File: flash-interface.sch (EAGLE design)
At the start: 2 parts, among them IC1 STM32L412K8U6, IC2 W25N01GVZEIG_TR

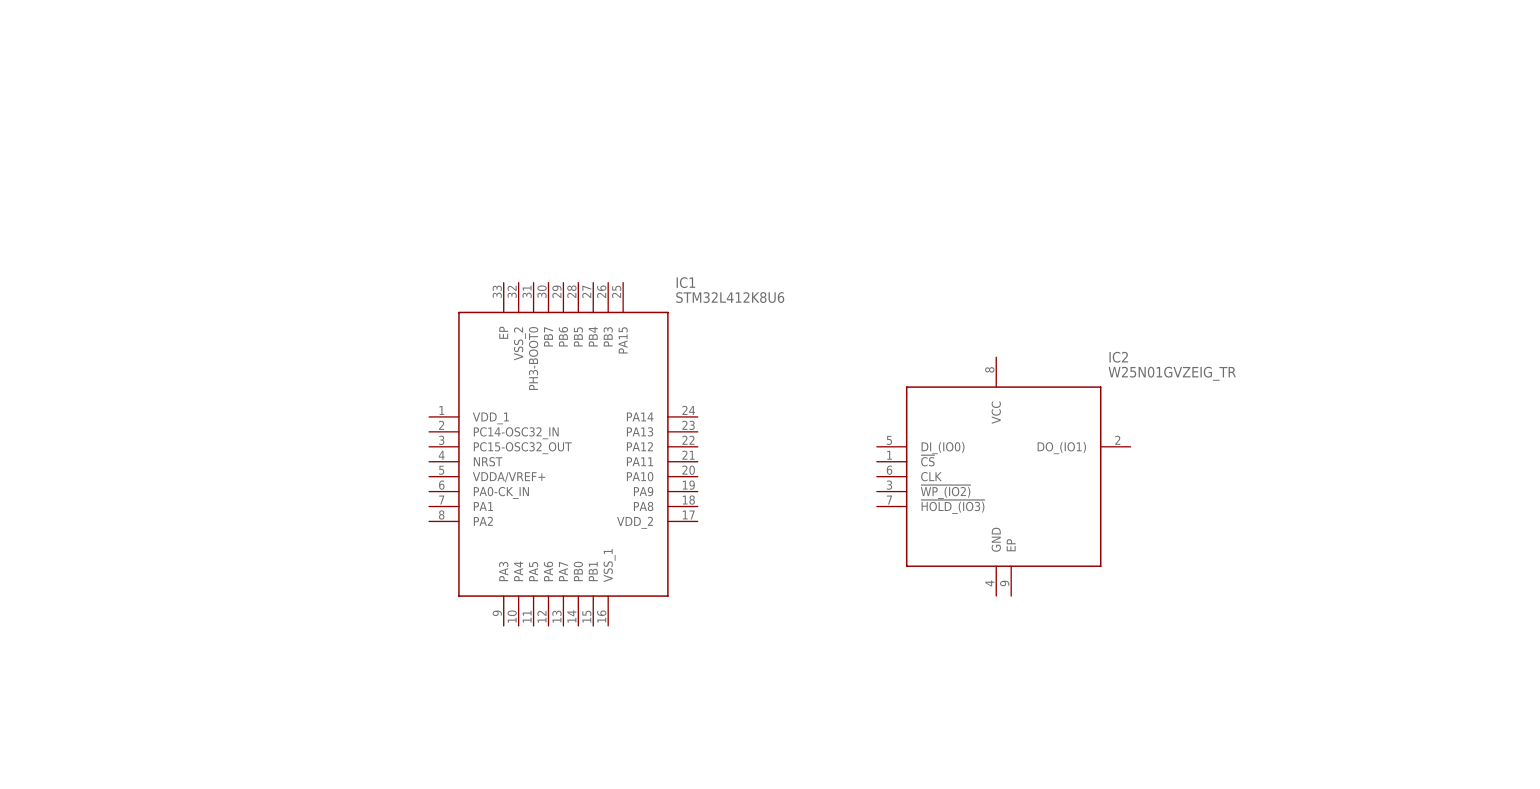
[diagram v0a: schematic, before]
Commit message: Added bare minimum components for both ICs
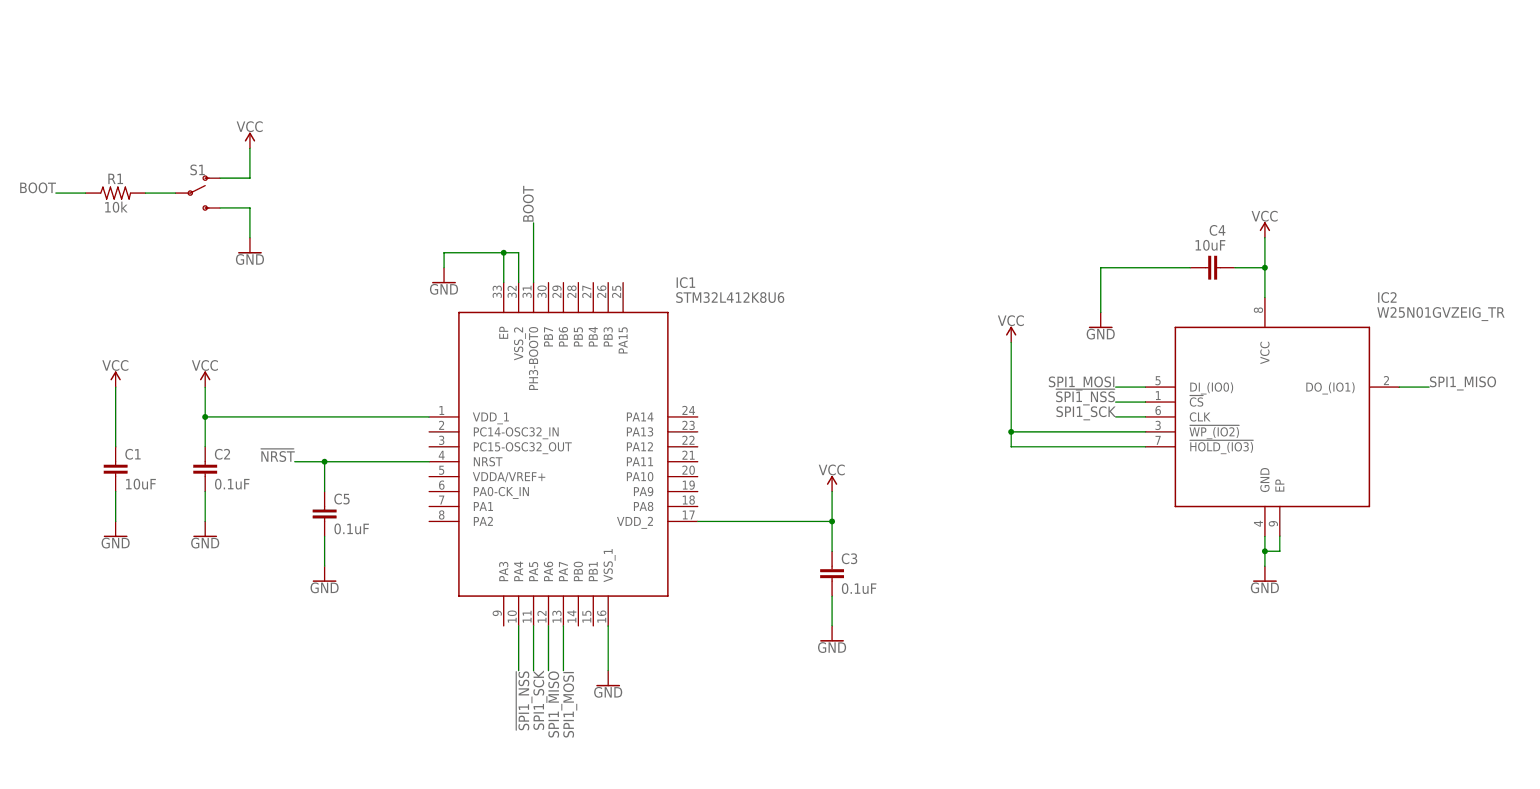
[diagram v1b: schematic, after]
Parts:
- added C1, C4: 10uF, SparkFun-Capacitors:10UF-0603-6.3V-20%
- added C2, C3, C5: 0.1uF, SparkFun-Capacitors:0.1UF-0603-25V-(+80/-20%)
- added R1: 10k, SparkFun-Resistors:10KOHM-0603-1/10W-1%
- added S1: (no value), SparkFun-Switches:SWITCH-SPDT-SMD-AYZ0202
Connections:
- new net !NRST: C5.1, IC1.NRST
- new net !SPI1_NSS: IC1.PA4, IC2.!CS
- new net BOOT: IC1.PH3-BOOT0, R1.1
- new net GND: C1.2, C2.2, C3.2, C4.2, C5.2, IC1.EP, IC1.VSS_1, IC1.VSS_2, IC2.EP, IC2.GND, S1.S
- new net N$1: R1.2, S1.P
- new net SPI1_MISO: IC1.PA6, IC2.DO_(IO1)
- new net SPI1_MOSI: IC1.PA7, IC2.DI_(IO0)
- new net SPI1_SCK: IC1.PA5, IC2.CLK
- new net VCC: C1.1, C2.1, C3.1, C4.1, IC1.VDD_1, IC1.VDD_2, IC2.!HOLD_(IO3), IC2.!WP_(IO2), IC2.VCC, S1.O
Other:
- moved on the sheet: IC2

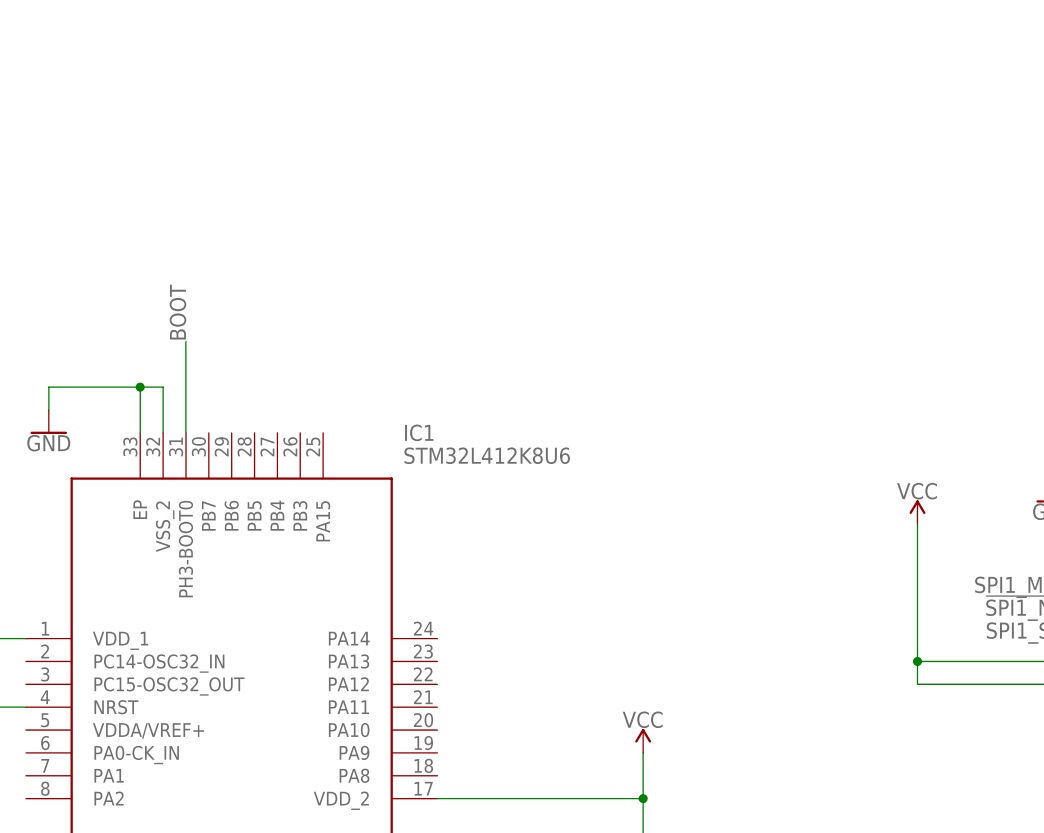
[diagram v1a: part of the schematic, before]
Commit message: Added SWD debug connector to STM32
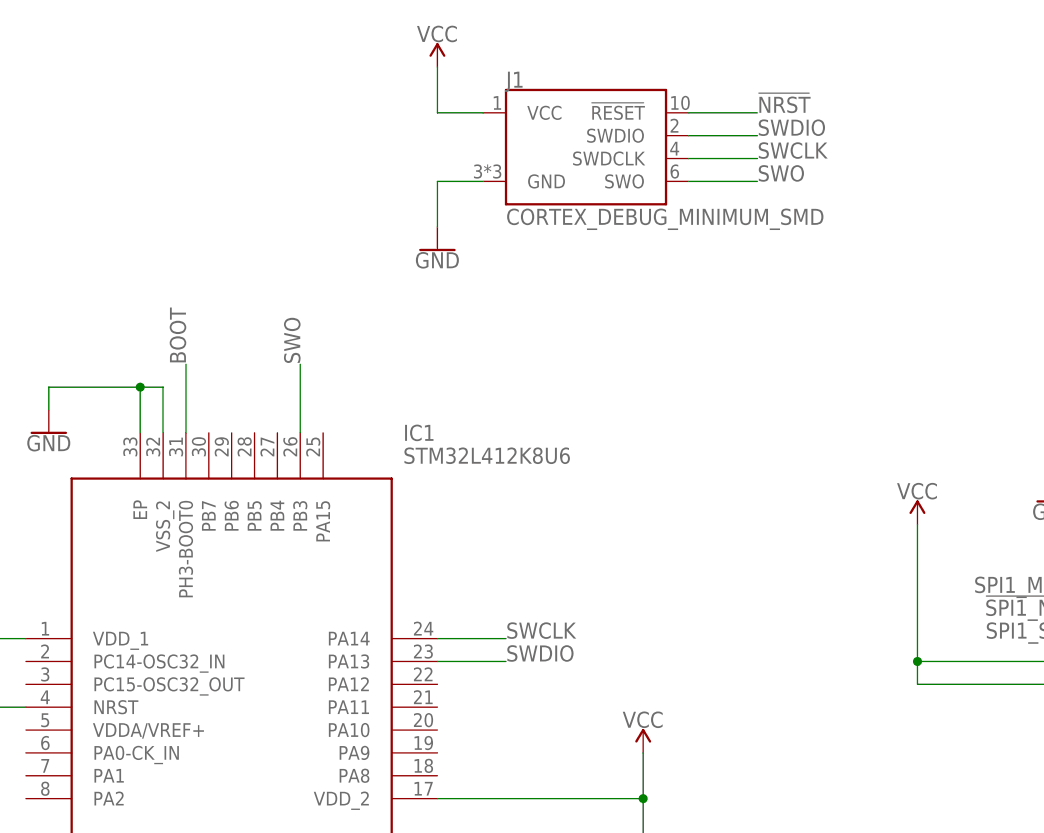
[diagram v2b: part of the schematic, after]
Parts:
- added J1: CORTEX_DEBUG_MINIMUM_SMD, SparkFun-Connectors:CORTEX_DEBUG_MINIMUM_SMD
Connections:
- new net SWCLK: IC1.PA14, J1.SWDCLK
- new net SWDIO: IC1.PA13, J1.SWDIO
- new net SWO: IC1.PB3, J1.SWO
- net !NRST: now also J1.!RESET
- net GND: now also J1.GND
- net VCC: now also J1.VCC
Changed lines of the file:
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@@
 <layer number="230" name="230bmp" color="7" fill="1" visible="yes" active="yes"/>
 <layer number="231" name="231bmp" color="7" fill="1" visible="yes" active="yes"/>
+<layer number="232" name="Eagle3D_PG2" color="7" fill="1" visible="no" active="no"/>
+<layer number="233" name="Eagle3D_PG3" color="7" fill="1" visible="no" active="no"/>
 <layer number="248" name="Housing" color="7" fill="1" visible="yes" active="yes"/>
 <layer number="249" name="Edge" color="7" fill="1" visible="yes" active="yes"/>
@@
 <part name="SUPPLY6" library="SparkFun-PowerSymbols" library_urn="urn:adsk.eagle:library:530" deviceset="VCC" device=""/>
 <part name="GND9" library="SparkFun-PowerSymbols" library_urn="urn:adsk.eagle:library:530" deviceset="GND" device=""/>
+<part name="J1" library="SparkFun-Connectors" deviceset="CORTEX_DEBUG_MINIMUM" device="_SMD"/>
+<part name="GND10" library="SparkFun-PowerSymbols" library_urn="urn:adsk.eagle:library:530" deviceset="GND" device=""/>
+<part name="SUPPLY7" library="SparkFun-PowerSymbols" library_urn="urn:adsk.eagle:library:530" deviceset="VCC" device=""/>
 </parts>
 <sheets>
@@
 <attribute name="VALUE" x="5.08" y="83.566" size="1.778" layer="96" align="top-center"/>
 </instance>
+<instance part="J1" gate="G$1" x="99.06" y="109.22" smashed="yes">
+<attribute name="NAME" x="88.9" y="117.094" size="1.778" layer="95" font="vector"/>
+<attribute name="VALUE" x="88.9" y="101.854" size="1.778" layer="96" font="vector"/>
+</instance>
+<instance part="GND10" gate="1" x="81.28" y="99.06" smashed="yes">
+<attribute name="VALUE" x="81.28" y="98.806" size="1.778" layer="96" align="top-center"/>
+</instance>
+<instance part="SUPPLY7" gate="G$1" x="81.28" y="119.38" smashed="yes">
+<attribute name="VALUE" x="81.28" y="122.174" size="1.778" layer="96" align="bottom-center"/>
+</instance>
 </instances>
 <busses>
@@
 <pinref part="GND9" gate="1" pin="GND"/>
 </segment>
+<segment>
+<pinref part="GND10" gate="1" pin="GND"/>
+<wire x1="81.28" y1="101.6" x2="81.28" y2="106.68" width="0.1524" layer="91"/>
+<pinref part="J1" gate="G$1" pin="GND"/>
+<wire x1="81.28" y1="106.68" x2="86.36" y2="106.68" width="0.1524" layer="91"/>
+</segment>
 </net>
 <net name="VCC" class="0">
@@
 <pinref part="SUPPLY6" gate="G$1" pin="VCC"/>
 </segment>
+<segment>
+<pinref part="SUPPLY7" gate="G$1" pin="VCC"/>
+<wire x1="81.28" y1="119.38" x2="81.28" y2="114.3" width="0.1524" layer="91"/>
+<pinref part="J1" gate="G$1" pin="VCC"/>
+<wire x1="81.28" y1="114.3" x2="86.36" y2="114.3" width="0.1524" layer="91"/>
+</segment>
 </net>
 <net name="!NRST" class="0">
@@
 <label x="12.7" y="48.26" size="1.778" layer="95" rot="MR0"/>
 </segment>
+<segment>
+<pinref part="J1" gate="G$1" pin="!RESET"/>
+<wire x1="109.22" y1="114.3" x2="116.84" y2="114.3" width="0.1524" layer="91"/>
+<label x="116.84" y="114.3" size="1.778" layer="95"/>
+</segment>
 </net>
 <net name="BOOT" class="0">
 <segment>
 <pinref part="IC1" gate="G$1" pin="PH3-BOOT0"/>
-<wire x1="53.34" y1="78.74" x2="53.34" y2="88.9" width="0.1524" layer="91"/>
-<label x="53.34" y="88.9" size="1.778" layer="95" rot="R90"/>
+<wire x1="53.34" y1="78.74" x2="53.34" y2="86.36" width="0.1524" layer="91"/>
+<label x="53.34" y="86.36" size="1.778" layer="95" rot="R90"/>
 </segment>
 <segment>
@@
 </segment>
 </net>
+<net name="SWDIO" class="0">
+<segment>
+<pinref part="IC1" gate="G$1" pin="PA13"/>
+<wire x1="81.28" y1="53.34" x2="88.9" y2="53.34" width="0.1524" layer="91"/>
+<label x="88.9" y="53.34" size="1.778" layer="95"/>
+</segment>
+<segment>
+<pinref part="J1" gate="G$1" pin="SWDIO"/>
+<wire x1="109.22" y1="111.76" x2="116.84" y2="111.76" width="0.1524" layer="91"/>
+<label x="116.84" y="111.76" size="1.778" layer="95"/>
+</segment>
+</net>
+<net name="SWCLK" class="0">
+<segment>
+<pinref part="IC1" gate="G$1" pin="PA14"/>
+<wire x1="81.28" y1="55.88" x2="88.9" y2="55.88" width="0.1524" layer="91"/>
+<label x="88.9" y="55.88" size="1.778" layer="95"/>
+</segment>
+<segment>
+<pinref part="J1" gate="G$1" pin="SWDCLK"/>
+<wire x1="109.22" y1="109.22" x2="116.84" y2="109.22" width="0.1524" layer="91"/>
+<label x="116.84" y="109.22" size="1.778" layer="95"/>
+</segment>
+</net>
+<net name="SWO" class="0">
+<segment>
+<pinref part="IC1" gate="G$1" pin="PB3"/>
+<wire x1="66.04" y1="78.74" x2="66.04" y2="86.36" width="0.1524" layer="91"/>
+<label x="66.04" y="86.36" size="1.778" layer="95" rot="R90"/>
+</segment>
+<segment>
+<pinref part="J1" gate="G$1" pin="SWO"/>
+<wire x1="109.22" y1="106.68" x2="116.84" y2="106.68" width="0.1524" layer="91"/>
+<label x="116.84" y="106.68" size="1.778" layer="95"/>
+</segment>
+</net>

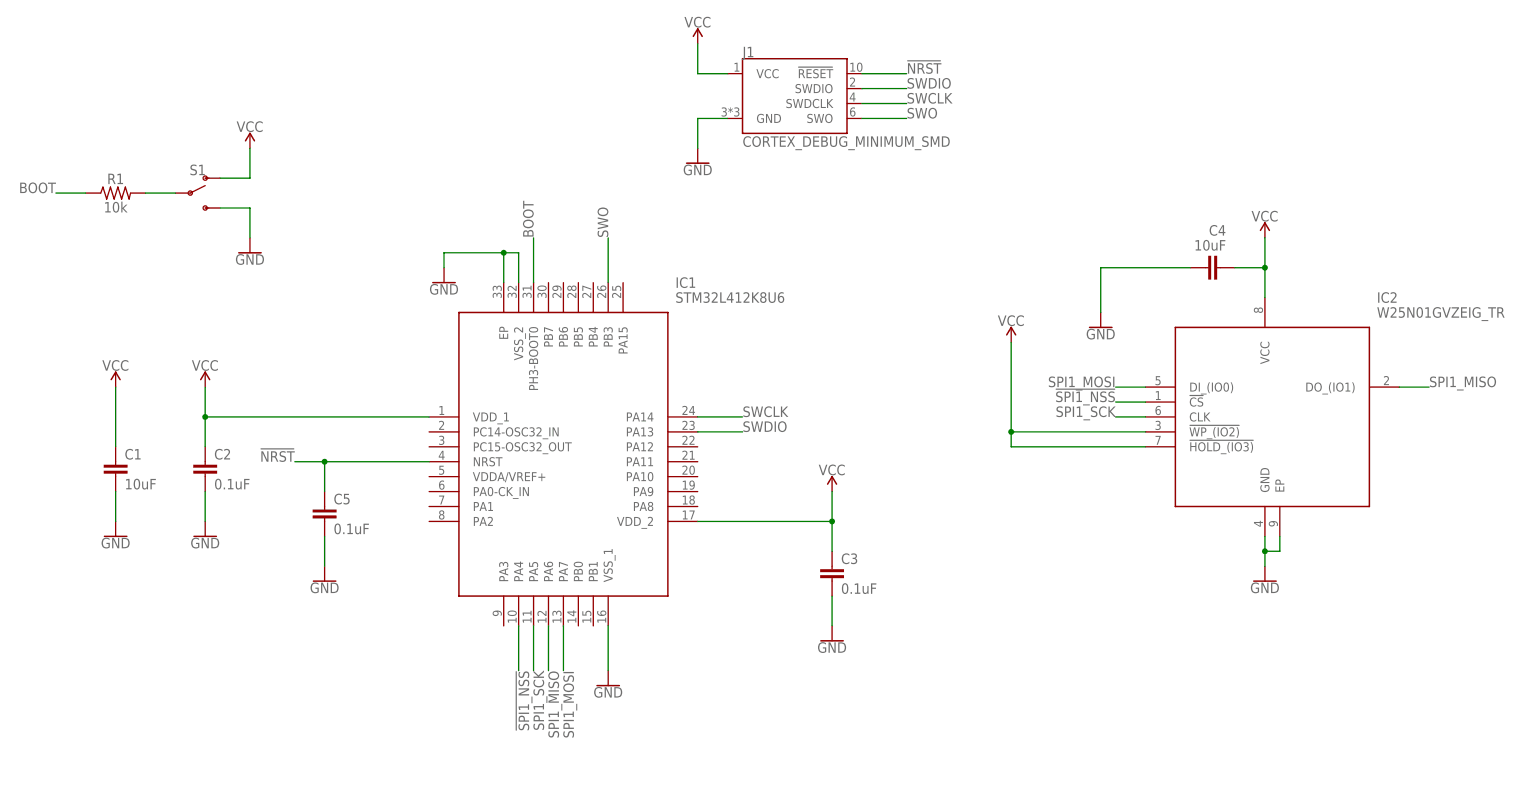
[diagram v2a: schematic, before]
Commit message: Replaced STM32 system with a Raspberry Pi SPI header
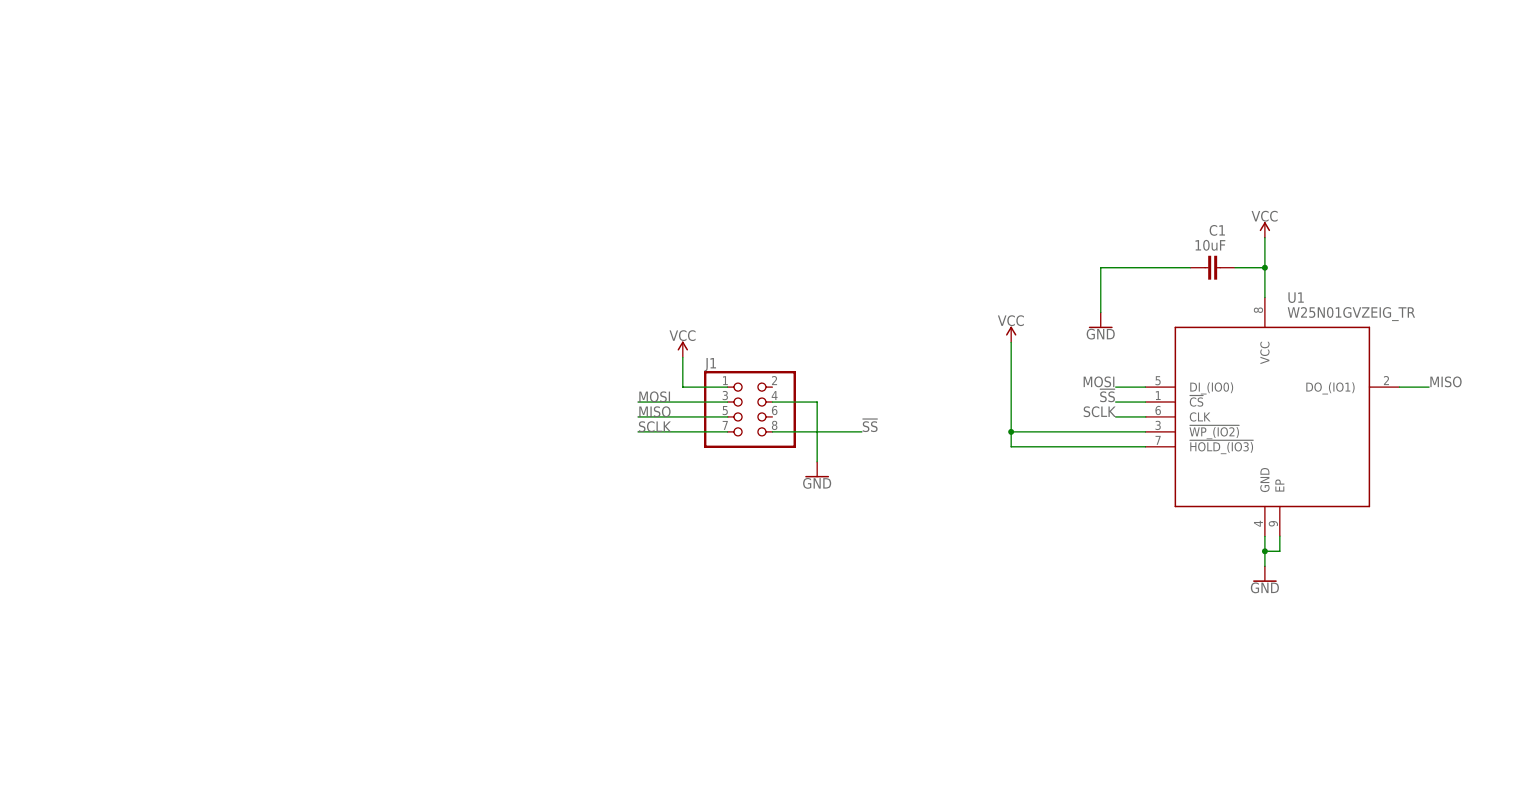
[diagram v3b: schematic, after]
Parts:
- removed C2, C3, C5: 0.1uF, SparkFun-Capacitors:0.1UF-0603-25V-(+80/-20%)
- removed C4: 10uF, SparkFun-Capacitors:10UF-0603-6.3V-20%
- removed IC1: STM32L412K8U6, flash-interface:STM32L412K8U6
- removed R1: 10k, SparkFun-Resistors:10KOHM-0603-1/10W-1%
- removed S1: (no value), SparkFun-Switches:SWITCH-SPDT-SMD-AYZ0202
- J1: value CORTEX_DEBUG_MINIMUM_SMD -> (none); device SparkFun-Connectors:CORTEX_DEBUG_MINIMUM_SMD -> pinhead:PINHD-2X4
- renumbered IC2 to U1
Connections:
- removed net !NRST: C5.1, IC1.NRST, J1.!RESET
- removed net !SPI1_NSS: IC1.PA4, U1.!CS
- removed net BOOT: IC1.PH3-BOOT0, R1.1
- removed net N$1: R1.2, S1.P
- removed net SPI1_MISO: IC1.PA6, U1.DO_(IO1)
- removed net SPI1_MOSI: IC1.PA7, U1.DI_(IO0)
- removed net SPI1_SCK: IC1.PA5, U1.CLK
- removed net SWCLK: IC1.PA14, J1.SWDCLK
- removed net SWDIO: IC1.PA13, J1.SWDIO
- removed net SWO: IC1.PB3, J1.SWO
- new net !SS: J1.8, U1.!CS
- new net MISO: J1.5, U1.DO_(IO1)
- new net MOSI: J1.3, U1.DI_(IO0)
- new net SCLK: J1.7, U1.CLK
- net GND: now also J1.4; no longer C2.2, C3.2, C4.2, C5.2, IC1.EP, IC1.VSS_1, IC1.VSS_2, J1.GND, S1.S
- net VCC: now also J1.1; no longer C2.1, C3.1, C4.1, IC1.VDD_1, IC1.VDD_2, J1.VCC, S1.O
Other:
- moved on the sheet: C1
